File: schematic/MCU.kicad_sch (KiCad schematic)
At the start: 13 parts, among them U15 STM32F767VGT6, U8 GPTS203211B

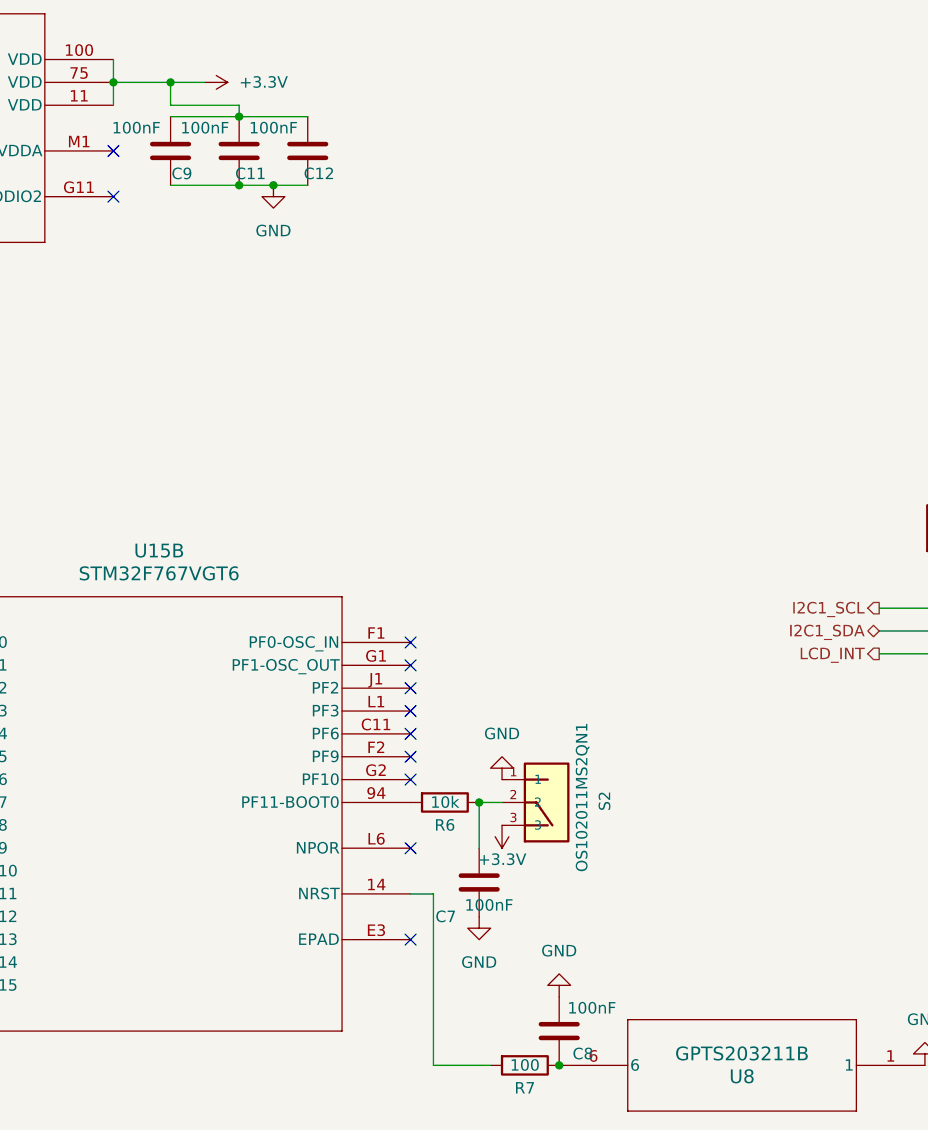
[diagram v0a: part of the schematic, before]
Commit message: Changed to Kicad Version 8
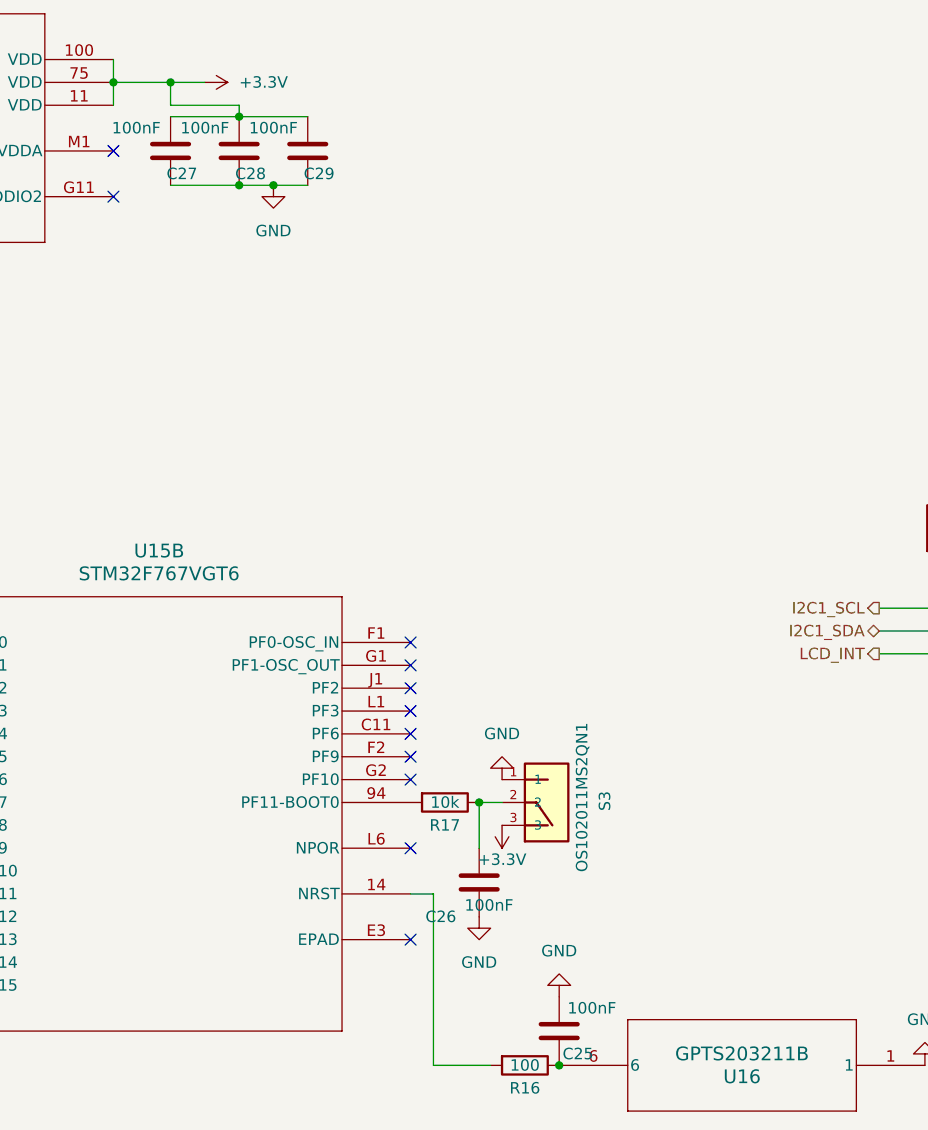
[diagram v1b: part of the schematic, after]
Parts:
- renumbered C8 to C25, C7 to C26, C9 to C27, C11 to C28, C12 to C29, R7 to R16, R6 to R17, S2 to S3, U8 to U16
